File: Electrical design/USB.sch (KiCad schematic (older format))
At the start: 15 parts

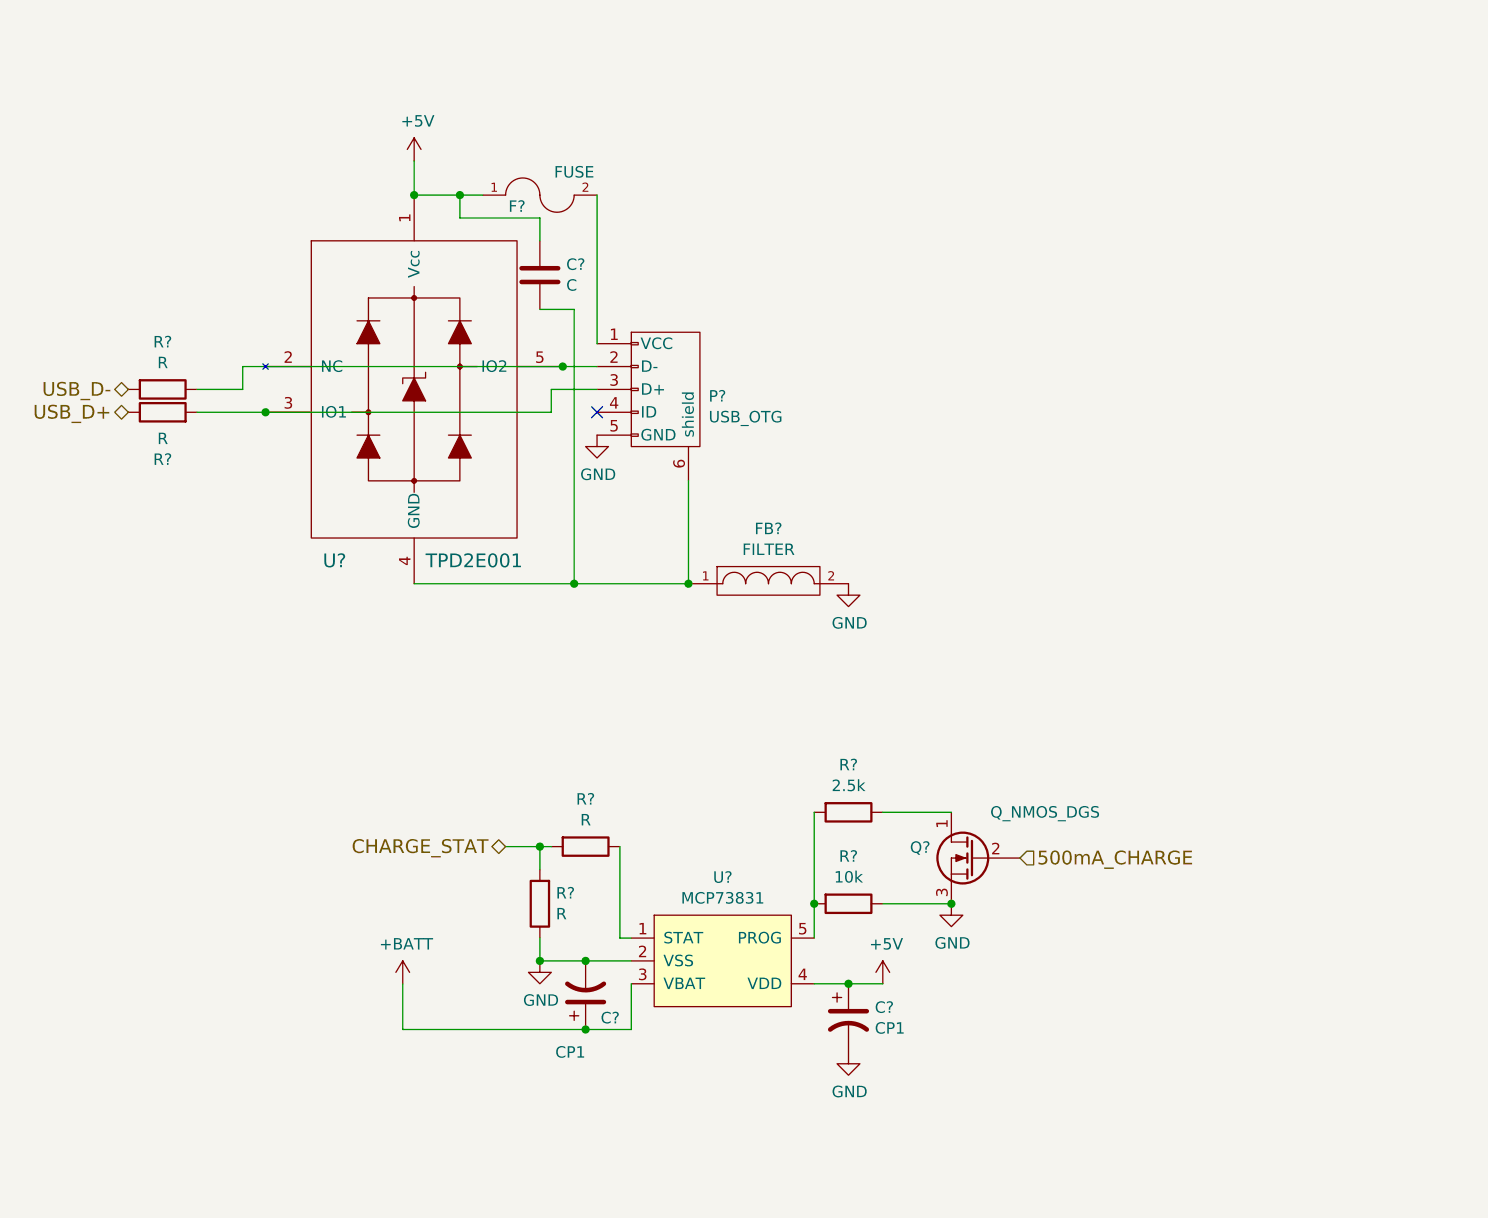
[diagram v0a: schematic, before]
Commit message: Updated schematics.
Added speaker / buzzer, reset circuit (battery under-voltage lockout), changed battery charger IC.
Altered Vout circuit.
Added most resistor / capacitor values (those missing are either dependent on battery thermistor or ADC).
Updated to show "correct" op-amps.
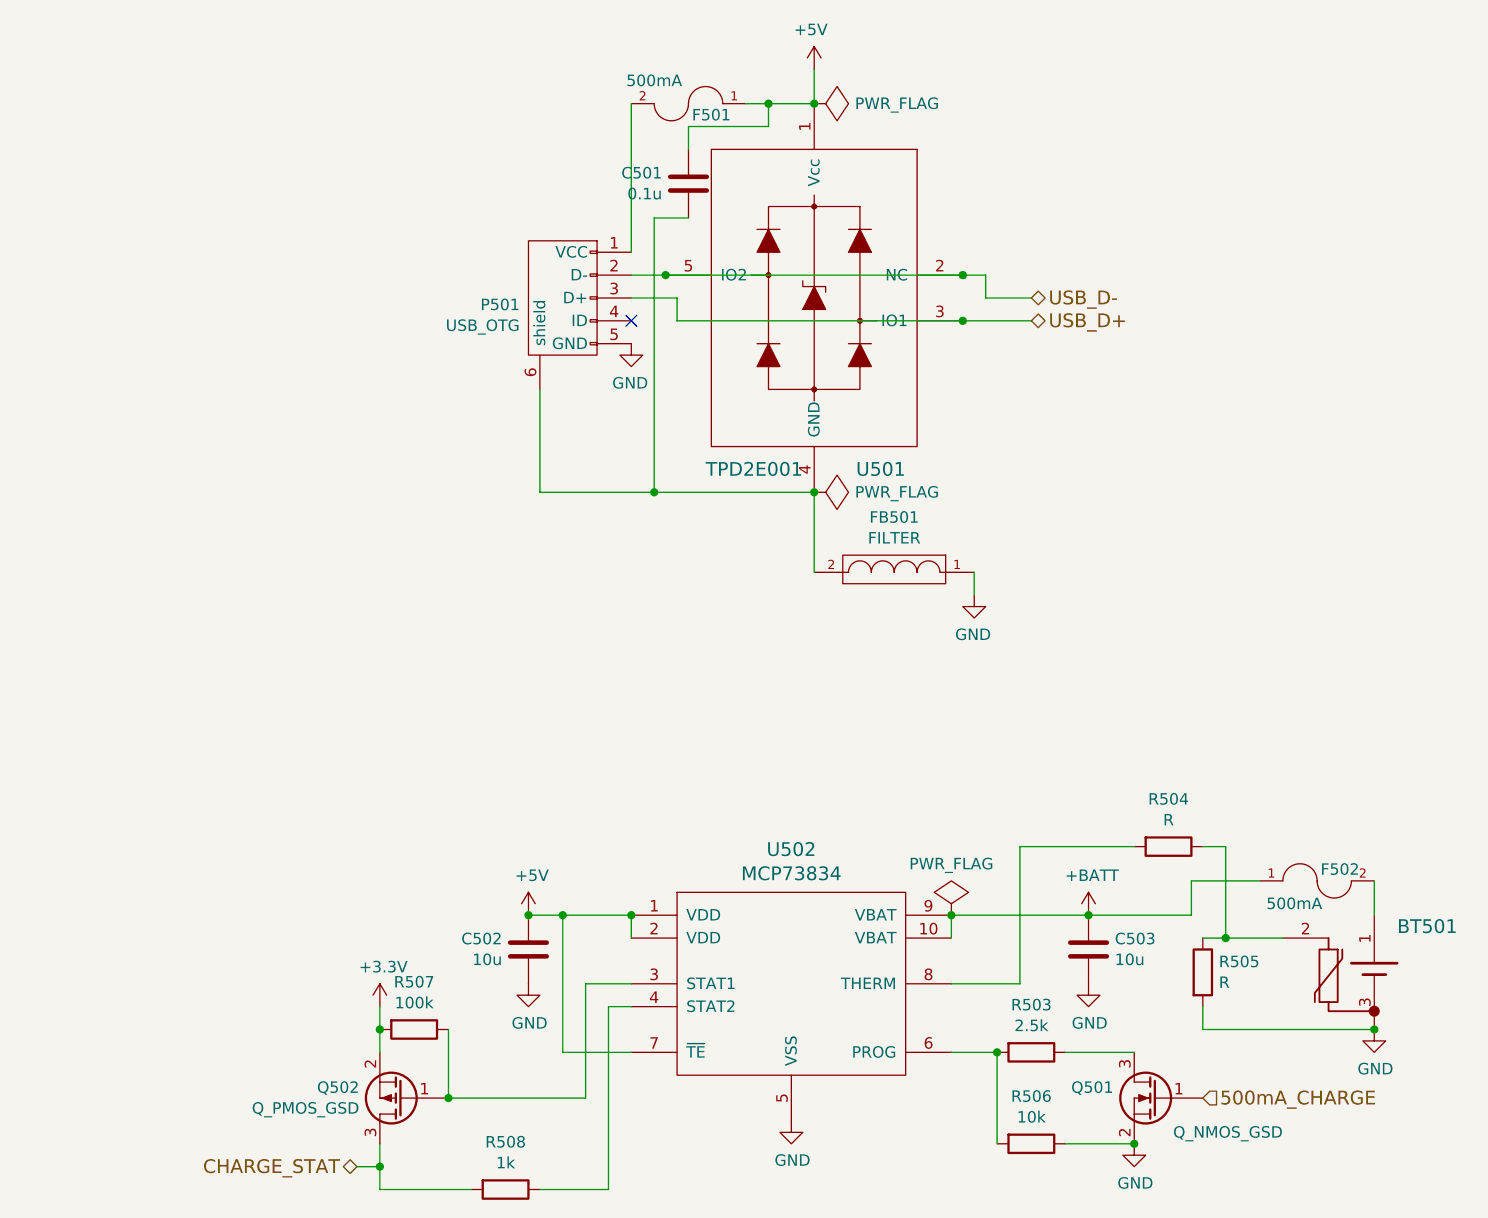
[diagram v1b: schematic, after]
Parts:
- removed C? (x2): CP1, symbol CP1
- removed Q?: Q_NMOS_DGS, symbol Q_NMOS_DGS
- removed R? (x4): R, symbol R
- removed U?: MCP73831, symbol MCP73831
- added BT501: Li-Ion_Cell, Pin_Headers:Pin_Header_Straight_1x03, symbol Li-Ion_Cell
- added C502, C503: 10u, my footprints:SMDuniversal_0603to1210_HandSoldering, symbol C
- added F502: 500mA, Resistors_SMD:R_1210_HandSoldering, symbol FUSE
- added Q501: Q_NMOS_GSD, TO_SOT_Packages_SMD:SOT-23, symbol Q_NMOS_GSD
- added Q502: Q_PMOS_GSD, TO_SOT_Packages_SMD:SOT-23, symbol Q_PMOS_GSD
- added R504, R505: R, my footprints:SMDuniversal_0603to1210_HandSoldering, symbol R
- added R507: 100k, my footprints:SMDuniversal_0603to1210_HandSoldering, symbol R
- added R508: 1k, my footprints:SMDuniversal_0603to1210_HandSoldering, symbol R
- added U502: MCP73834, my footprints:MSOP-10_3x3mm_Pitch0.5mm, symbol MCP73834
- C501: renamed from C?; value C -> 0.1u; footprint (none) -> my footprints:SMDuniversal_0603to1210_HandSoldering
- F501: renamed from F?; value FUSE -> 500mA; footprint (none) -> Resistors_SMD:R_1210_HandSoldering
- FB501: renamed from FB?; footprint (none) -> my footprints:SMDuniversal_0603to1210_HandSoldering
- P501: renamed from P?; footprint (none) -> my footprints:MicroUSB_B_Vertical
- R503, R506: renamed from R?; footprint (none) -> my footprints:SMDuniversal_0603to1210_HandSoldering
- U501: renamed from U?; footprint (none) -> my footprints:VSOF5_HandSoldering
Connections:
- net +5V: now also C502.1, U502.1 (VDD), U502.2 (VDD), U502.7 (~TE)
- net +BATT: now also C503.1, F502.1, U502.10 (VBAT), U502.9 (VBAT)
- net 500mA_CHARGE: now also Q501.1 (G)
- net CHARGE_STAT: now also Q502.3 (D), R508.2
- net GND: now also FB501.1, BT501.3, C502.2, C503.2, Q501.2 (S), R505.2, U502.5 (VSS); no longer FB501.2
- net USB_D+: now also P501.3 (D+), U501.3 (IO1)
- net USB_D-: now also P501.2 (D-), U501.2 (NC), U501.5 (IO2)
- net at C501.1, P501.6 (shield), U501.4 (GND): now also FB501.2; no longer FB501.1
- net at R503.2, R506.2: now also U502.6 (PROG)
- net at R503.1: now also Q501.3 (D)
- new net: Q502.1 (G), R507.1, U502.3 (STAT1)
- new net: R508.1, U502.4 (STAT2)
- new net: R504.2, U502.8 (THERM)
- new net: BT501.1, F502.2
- new net: BT501.2, R504.1, R505.1
- new net +3V3: Q502.2 (S), R507.2
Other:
- moved on the sheet: C501, F501, FB501, P501, R503, R506, U501

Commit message: Update External Design. Add battery sense capacitor. Update footprints.
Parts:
- C501: footprint my footprints:SMDuniversal_0603to1210_HandSoldering -> my footprints:SMDuniversal_0603to0805_HandSoldering
- C502, C503: footprint my footprints:SMDuniversal_0603to1210_HandSoldering -> my footprints:SMDuniversal_0603to1206_HandSoldering
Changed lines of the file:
@@
 Sheet 5 5
 Title "USB and charging"
-Date ""
-Rev ""
+Date "2016-06-22"
+Rev "0.5"
 Comp ""
 Comment1 ""
@@
 F 0 "C501" H 4535 1554 50  0000 R CNN
 F 1 "0.1u" H 4535 1645 50  0000 R CNN
-F 2 "my footprints:SMDuniversal_0603to1210_HandSoldering" H 4688 1450 50  0001 C CNN
+F 2 "my footprints:SMDuniversal_0603to0805_HandSoldering" H 4688 1450 50  0001 C CNN
 F 3 "" H 4650 1600 50  0000 C CNN
 	1    4650 1600
@@
 F 0 "C502" H 4065 4996 50  0000 L CNN
 F 1 "10u" H 4065 4905 50  0000 L CNN
-F 2 "my footprints:SMDuniversal_0603to1210_HandSoldering" H 3988 4800 50  0001 C CNN
+F 2 "my footprints:SMDuniversal_0603to1206_HandSoldering" H 3988 4800 50  0001 C CNN
 F 3 "" H 3950 4950 50  0000 C CNN
 	1    3950 4950
@@
 F 0 "C503" H 6515 4996 50  0000 L CNN
 F 1 "10u" H 6515 4905 50  0000 L CNN
-F 2 "my footprints:SMDuniversal_0603to1210_HandSoldering" H 6438 4800 50  0001 C CNN
+F 2 "my footprints:SMDuniversal_0603to1206_HandSoldering" H 6438 4800 50  0001 C CNN
 F 3 "" H 6400 4950 50  0000 C CNN
 	1    6400 4950
